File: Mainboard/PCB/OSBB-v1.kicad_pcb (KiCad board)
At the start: 2 copper layers, 85.6 x 49.8 mm, 150 parts, among them P1 AUX 1-3, P14 EXTRA Pins, P2 Wire to Teensy VUSB, P3 +3.3V, P4 Pit Limiter, P5 Rotary Encoders, P6 BTN 1-32, P7 LED, Q1 NPN, Q2 NPN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

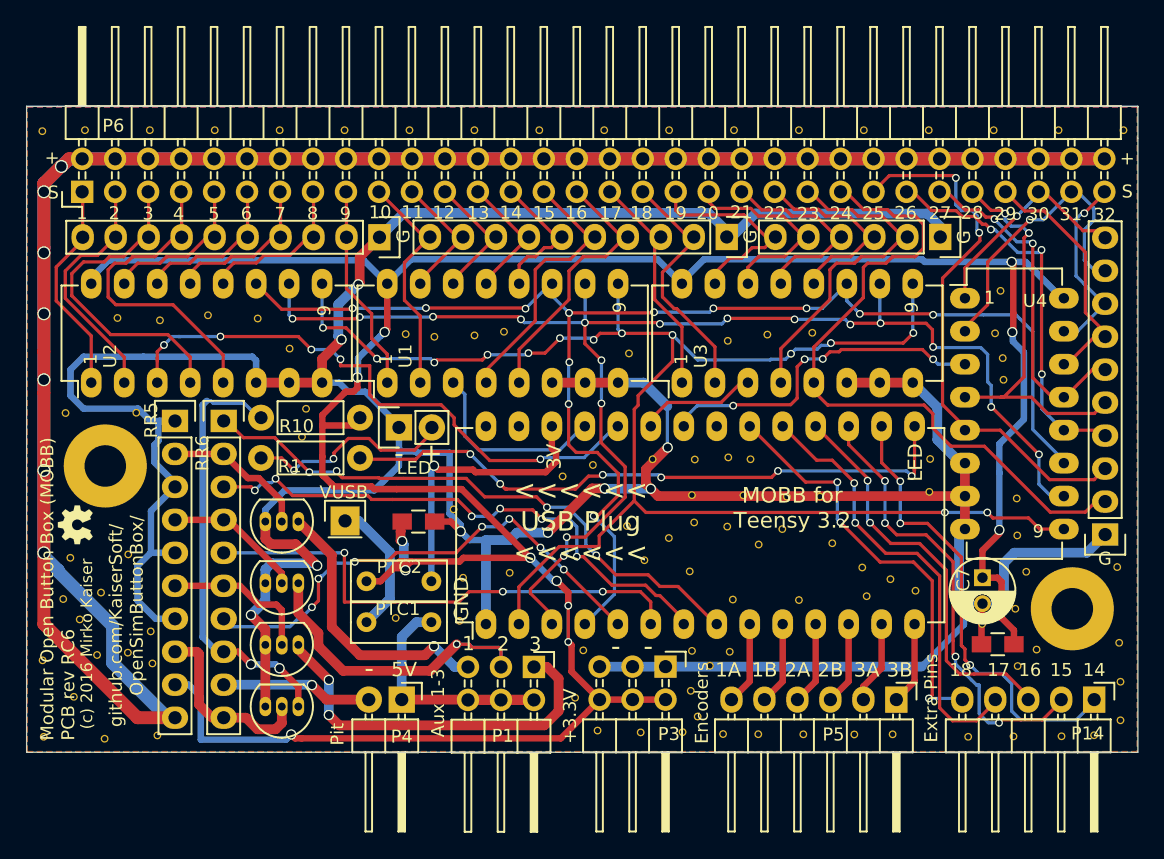
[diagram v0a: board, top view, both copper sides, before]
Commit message: * updated schematic for version 1.0   from RC6   * adjusted silkscreen positions   * replaced RR6 and RR5 footprint, removed pin 1 indicator   * C4 now through hole   * removed vias from 32pin supply line
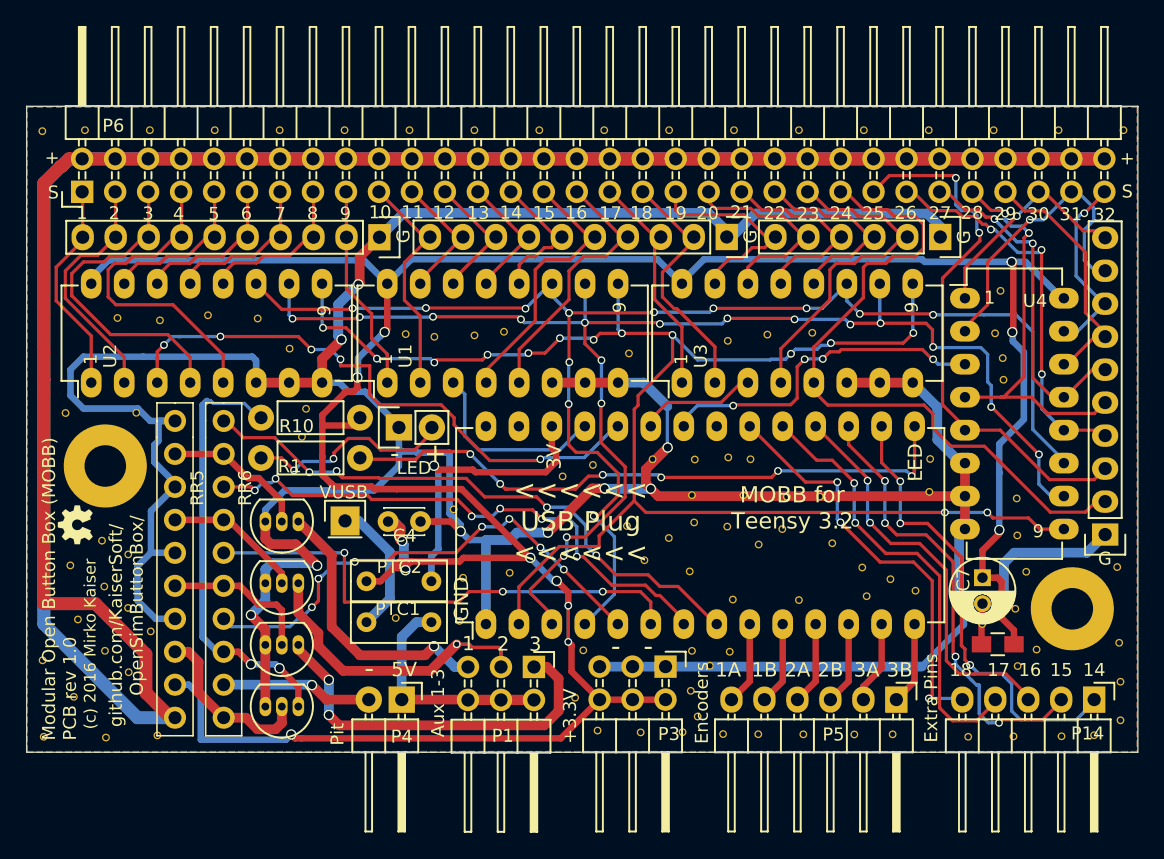
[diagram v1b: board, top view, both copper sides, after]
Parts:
- C4: footprint Capacitors_SMD:C_0805_HandSoldering -> Capacitors_ThroughHole:C_Disc_D3.0mm_W2.0mm_P2.50mm
- RR5: value 10K-STAR10 -> 10K-NETWORK; footprint Pin_Headers:Pin_Header_Straight_1x10 -> MOBB-KiCad-Lib:Resistor_Network-1x10
- RR6: value 1K-STAR10 -> 1K-NETWORK; footprint Pin_Headers:Pin_Header_Straight_1x10 -> MOBB-KiCad-Lib:Resistor_Network-1x10
- moved G*** 7.82 mm to (181.5, 140.3)
- moved Ref** 6.31 mm to (181.1, 128.5)
- moved G*** 5.68 mm to (217.2, 129.4)
- moved Ref** 4.67 mm to (183.1, 133.7)
- moved Ref** 1.94 mm to (179.3, 134.5)
- moved Ref** 1.51 mm to (183.2, 138.6)
- moved Ref** 0.69 mm to (181.4, 137.0)
- moved Ref** 0.58 mm to (178.7, 130.4)
- moved Ref** 0.53 mm to (181.3, 132.0)
- moved C4 0.16 mm to (205.7, 127.0)
- moved Ref** 0.14 mm to (181.4, 143.6)
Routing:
- net PINHEADERSRC: track 334.5 -> 337.2 mm, vias 7 -> 0
- net +3V3: track 236.6 -> 238.3 mm
- net GND: track 312.8 -> 313.9 mm
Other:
- board text added: "Modular Open Button Box (MOBB) PCB rev 1.0"
- board text removed: "Modular Open Button Box (MOBB) PCB rev RC6"
